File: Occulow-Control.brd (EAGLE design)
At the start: 38.1 x 101.6 mm, 40 parts, among them J1 CORTEX_DEBUG_PTH, T1 DMP3010LK3, T2 DMP3010LK3, T3 DMP3010LK3

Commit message: Move schematic grideye pins to i2c pads, fixes #2
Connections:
- net GR_INT_HDR: now also U$1.13; no longer U$1.14
- net GR_SCL_HDR: now also U$1.12; no longer U$1.13
- net GR_SDA_HDR: now also U$1.11; no longer U$1.12
- net GR_VCC_CTL: now also U$1.14; no longer U$1.11
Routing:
- net GR_INT_HDR: track 16.2 -> 0.00 mm
- net GR_SCL_HDR: track 15.5 -> 0.00 mm
- net GR_SDA_HDR: track 14.8 -> 0.00 mm
- net GR_VCC_CTL: track 11.7 -> 6.48 mm
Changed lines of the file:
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@@
 <signal name="GR_SDA_HDR">
 <contactref element="GRIDEYE_HDR" pad="1"/>
-<contactref element="U$1" pad="12"/>
-<wire x1="21.8165" y1="16.872" x2="23.73" y2="16.872" width="0.254" layer="1"/>
-<wire x1="23.73" y1="16.872" x2="28.321" y2="21.463" width="0.254" layer="1"/>
-<wire x1="28.321" y1="21.463" x2="34.671" y2="21.463" width="0.254" layer="1"/>
-<wire x1="34.671" y1="21.463" x2="34.7345" y2="21.3995" width="0.254" layer="1"/>
+<wire x1="23.73" y1="16.872" x2="28.321" y2="21.463" width="0" layer="19" extent="1-16"/>
+<wire x1="28.321" y1="21.463" x2="34.671" y2="21.463" width="0" layer="19" extent="1-16"/>
+<wire x1="34.671" y1="21.463" x2="34.7345" y2="21.3995" width="0" layer="19" extent="1-16"/>
+<contactref element="U$1" pad="11"/>
+<wire x1="21.8165" y1="16.072" x2="23.73" y2="16.872" width="0" layer="19" extent="1-1"/>
 </signal>
 <signal name="GR_SCL_HDR">
 <contactref element="GRIDEYE_HDR" pad="2"/>
-<contactref element="U$1" pad="13"/>
-<wire x1="21.8165" y1="17.672" x2="23.768" y2="17.672" width="0.254" layer="1"/>
-<wire x1="23.768" y1="17.672" x2="28.194" y2="22.098" width="0.254" layer="1"/>
-<wire x1="28.194" y1="22.098" x2="32.893" y2="22.098" width="0.254" layer="1"/>
-<wire x1="32.893" y1="22.098" x2="34.7345" y2="23.9395" width="0.254" layer="1"/>
+<contactref element="U$1" pad="12"/>
+<wire x1="21.8165" y1="16.872" x2="34.7345" y2="23.9395" width="0" layer="19" extent="1-1"/>
 </signal>
 <signal name="GR_INT_HDR">
 <contactref element="GRIDEYE_HDR" pad="3"/>
-<contactref element="U$1" pad="14"/>
-<wire x1="21.8165" y1="18.472" x2="23.806" y2="18.472" width="0.254" layer="1"/>
-<wire x1="23.806" y1="18.472" x2="27.94" y2="22.606" width="0.254" layer="1"/>
-<wire x1="27.94" y1="22.606" x2="30.861" y2="22.606" width="0.254" layer="1"/>
-<wire x1="30.861" y1="22.606" x2="34.7345" y2="26.4795" width="0.254" layer="1"/>
+<contactref element="U$1" pad="13"/>
+<wire x1="21.8165" y1="17.672" x2="34.7345" y2="26.4795" width="0" layer="19" extent="1-1"/>
 </signal>
 <signal name="GR_VCC_CTL">
 <contactref element="T2" pad="1"/>
-<contactref element="U$1" pad="11"/>
-<wire x1="21.8165" y1="16.072" x2="21.139" y2="16.072" width="0.254" layer="1"/>
-<wire x1="21.139" y1="16.072" x2="20.828" y2="16.383" width="0.254" layer="1"/>
-<wire x1="20.828" y1="16.383" x2="20.828" y2="20.447" width="0.254" layer="1"/>
+<wire x1="21.139" y1="16.072" x2="20.828" y2="16.383" width="0" layer="19" extent="1-16"/>
+<wire x1="20.828" y1="16.383" x2="20.828" y2="20.447" width="0" layer="19" extent="1-16"/>
 <wire x1="20.828" y1="20.447" x2="23.114" y2="22.733" width="0.254" layer="1"/>
 <wire x1="23.114" y1="22.733" x2="23.114" y2="24.531" width="0.254" layer="1"/>
 <wire x1="23.114" y1="24.531" x2="24.136" y2="25.553" width="0.254" layer="1"/>
+<contactref element="U$1" pad="14"/>
+<wire x1="20.828" y1="20.447" x2="21.8165" y2="18.472" width="0" layer="19" extent="1-1"/>
 </signal>
 <signal name="GR_VCC">

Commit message: Updated debug header, re-routed grideye header
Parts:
- removed J1: CORTEX_DEBUG_PTH, SparkFun-Connectors:2X5-PTH-1.27MM
- added U$5: CORTEX-ICE, cortex-debug:2X5-1.27MM
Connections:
- net !RESET: now also U$5.10; no longer J1.10
- net GND: now also U$5.3, U$5.5; no longer J1.3, J1.5
- net SWCLK: now also U$5.4; no longer J1.4
- net SWDIO: now also U$5.2; no longer J1.2
- net VCC: now also U$5.1; no longer J1.1
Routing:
- net GR_INT_HDR: track 0.00 -> 16.6 mm
- net GR_SDA_HDR: track 0.00 -> 16.0 mm
- net GR_SCL_HDR: track 0.00 -> 15.8 mm
- net GR_VCC_CTL: track 6.48 -> 9.30 mm
- net !RESET: track 21.1 -> 21.6 mm
- net SWDIO: track 12.1 -> 11.5 mm
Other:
- board text removed: "CORTEX DEBUG"

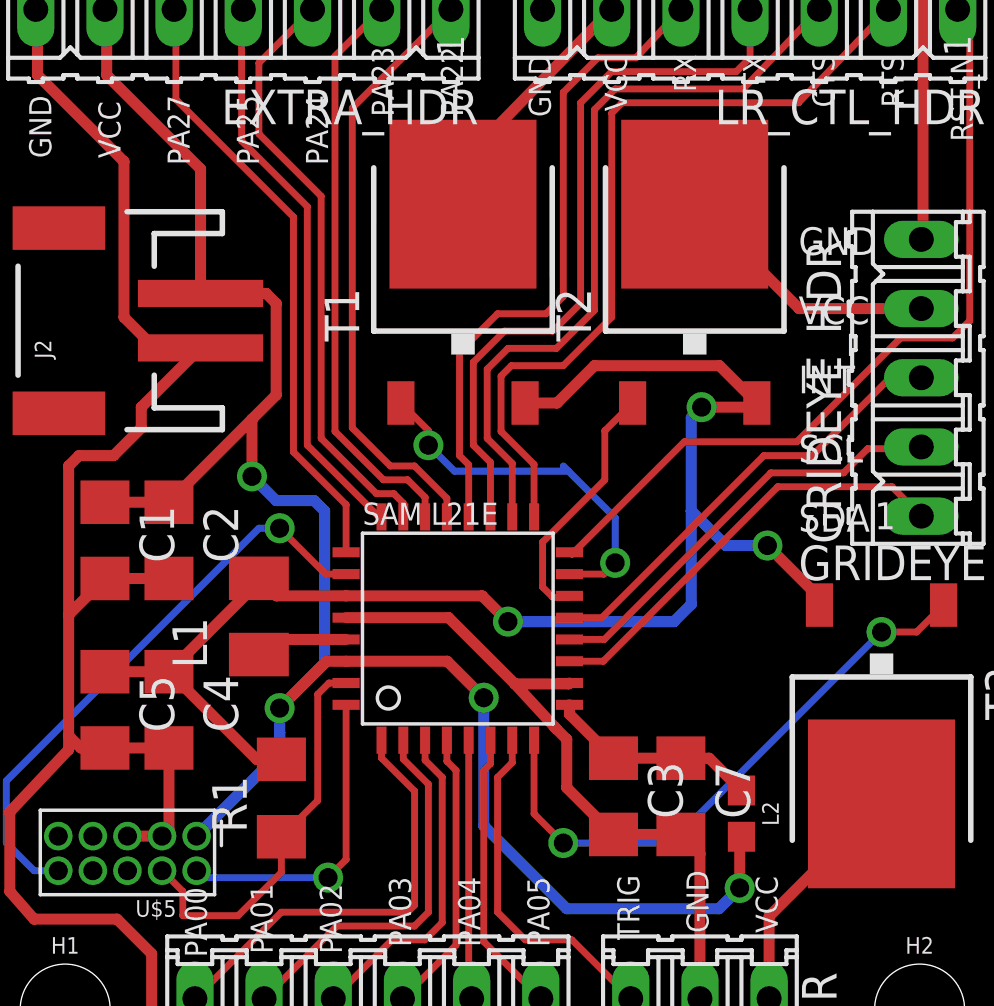
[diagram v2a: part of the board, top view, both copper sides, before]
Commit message: No VDDCORE power, all vcc. Fixes #9
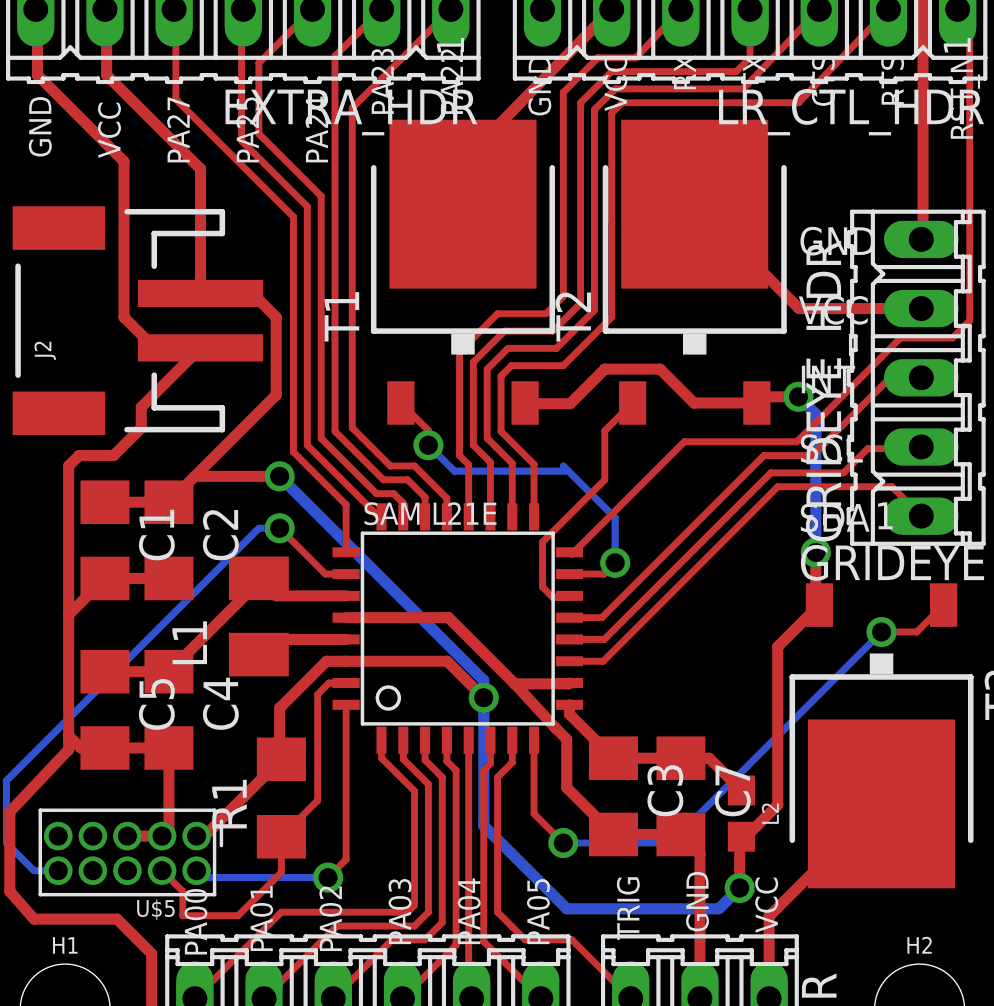
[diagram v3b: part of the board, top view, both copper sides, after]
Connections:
- net VCC: now also R1.2, T1.2, T2.2, T3.2
- net VDDCORE: no longer R1.2, T1.2, T2.2, T3.2
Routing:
- net VDDCORE: track 54.8 -> 10.6 mm, vias 3 -> 0
- net VCC: track 72.0 -> 101.6 mm, vias 4 -> 5
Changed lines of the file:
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@@
 <contactref element="EXTRA_HDR" pad="6"/>
 <wire x1="7.112" y1="21.9105" x2="4.7625" y2="21.9105" width="0.4064" layer="1"/>
-<wire x1="10.684" y1="29.575" x2="8.272" y2="29.575" width="0.4064" layer="1"/>
-<wire x1="10.684" y1="29.575" x2="11.049" y2="29.21" width="0.4064" layer="1"/>
-<wire x1="11.049" y1="29.21" x2="11.049" y2="25.8475" width="0.4064" layer="1"/>
-<wire x1="10.16" y1="24.9585" x2="11.049" y2="25.8475" width="0.4064" layer="1"/>
-<wire x1="10.16" y1="24.9585" x2="7.112" y2="21.9105" width="0.4064" layer="1"/>
-<wire x1="8.272" y1="29.575" x2="8.272" y2="34.146" width="0.4064" layer="1"/>
+<wire x1="8.272" y1="34.146" x2="8.272" y2="29.575" width="0.4064" layer="1"/>
 <wire x1="8.272" y1="34.146" x2="4.826" y2="37.592" width="0.4064" layer="1"/>
 <wire x1="4.826" y1="37.592" x2="4.826" y2="39.9415" width="0.4064" layer="1"/>
 <wire x1="4.826" y1="39.9415" x2="4.7625" y2="40.005" width="0.4064" layer="1"/>
-<wire x1="12.897" y1="16.072" x2="13.6165" y2="16.072" width="0.4064" layer="1"/>
-<wire x1="12.897" y1="16.072" x2="11.176" y2="14.351" width="0.4064" layer="1"/>
-<via x="11.176" y="14.351" extent="1-16" drill="0.7"/>
-<wire x1="11.176" y1="13.081" x2="11.176" y2="13.462" width="0.4064" layer="16"/>
-<via x="10.16" y="22.86" extent="1-16" drill="0.7"/>
-<wire x1="11.176" y1="13.462" x2="11.176" y2="14.351" width="0.4064" layer="16"/>
-<wire x1="10.16" y1="22.86" x2="10.16" y2="24.9585" width="0.4064" layer="1"/>
-<wire x1="11.176" y1="14.351" x2="12.827" y2="16.002" width="0.4064" layer="16"/>
-<wire x1="12.827" y1="16.002" x2="12.827" y2="21.59" width="0.4064" layer="16"/>
-<wire x1="12.827" y1="21.59" x2="12.446" y2="21.971" width="0.4064" layer="16"/>
-<wire x1="12.446" y1="21.971" x2="11.049" y2="21.971" width="0.4064" layer="16"/>
-<wire x1="11.049" y1="21.971" x2="10.16" y2="22.86" width="0.4064" layer="16"/>
-<wire x1="13.6165" y1="16.072" x2="17.329" y2="16.072" width="0.4064" layer="1"/>
+<wire x1="17.329" y1="16.072" x2="13.6165" y2="16.072" width="0.4064" layer="1"/>
 <wire x1="17.329" y1="16.072" x2="18.669" y2="14.732" width="0.4064" layer="1"/>
 <via x="18.669" y="14.732" extent="1-16" drill="0.7"/>
-<wire x1="18.669" y1="14.732" x2="18.669" y2="10.033" width="0.4064" layer="16"/>
+<wire x1="18.669" y1="10.033" x2="18.669" y2="14.732" width="0.4064" layer="16"/>
 <wire x1="18.669" y1="10.033" x2="21.717" y2="6.985" width="0.4064" layer="16"/>
 <wire x1="21.717" y1="6.985" x2="27.305" y2="6.985" width="0.4064" layer="16"/>
@@
 <wire x1="28.067" y1="9.564" x2="28.1305" y2="9.6275" width="0.4064" layer="1"/>
 <contactref element="U$5" pad="1"/>
-<wire x1="11.176" y1="13.462" x2="11.176" y2="12.7" width="0.4064" layer="16"/>
-<wire x1="11.176" y1="12.7" x2="8.128" y2="9.652" width="0.4064" layer="16"/>
+<contactref element="R1" pad="2"/>
+<contactref element="T1" pad="2"/>
+<contactref element="T2" pad="2"/>
+<contactref element="T3" pad="2"/>
+<wire x1="28.1305" y1="9.6275" x2="28.2965" y2="9.6275" width="0.4064" layer="1"/>
+<wire x1="28.2965" y1="9.6275" x2="29.464" y2="10.795" width="0.4064" layer="1"/>
+<wire x1="29.464" y1="10.795" x2="29.464" y2="16.605" width="0.4064" layer="1"/>
+<wire x1="30.994" y1="18.135" x2="29.464" y2="16.605" width="0.4064" layer="1"/>
+<wire x1="8.272" y1="29.575" x2="10.176" y2="29.575" width="0.4064" layer="1"/>
+<wire x1="10.176" y1="29.575" x2="11.049" y2="28.702" width="0.4064" layer="1"/>
+<wire x1="11.049" y1="28.702" x2="11.049" y2="25.8475" width="0.4064" layer="1"/>
+<wire x1="8.0615" y1="22.86" x2="11.049" y2="25.8475" width="0.4064" layer="1"/>
+<wire x1="8.0615" y1="22.86" x2="7.112" y2="21.9105" width="0.4064" layer="1"/>
+<wire x1="13.6165" y1="16.072" x2="12.897" y2="16.072" width="0.4064" layer="1"/>
+<wire x1="12.897" y1="16.072" x2="11.176" y2="14.351" width="0.4064" layer="1"/>
+<wire x1="11.176" y1="14.351" x2="11.176" y2="12.5345" width="0.4064" layer="1"/>
+<wire x1="11.2395" y1="12.471" x2="11.176" y2="12.5345" width="0.4064" layer="1"/>
+<wire x1="8.128" y1="9.652" x2="8.4205" y2="9.652" width="0.4064" layer="1"/>
+<wire x1="8.4205" y1="9.652" x2="11.2395" y2="12.471" width="0.4064" layer="1"/>
+<via x="30.861" y="20.066" extent="1-16" drill="0.7"/>
+<wire x1="30.861" y1="20.066" x2="30.861" y2="18.268" width="0.4064" layer="1"/>
+<wire x1="30.861" y1="18.268" x2="30.994" y2="18.135" width="0.4064" layer="1"/>
+<wire x1="30.861" y1="20.066" x2="30.861" y2="25.146" width="0.4064" layer="16"/>
+<wire x1="30.861" y1="25.146" x2="30.226" y2="25.781" width="0.4064" layer="16"/>
+<via x="30.226" y="25.781" extent="1-16" drill="0.7"/>
+<wire x1="30.226" y1="25.781" x2="28.924" y2="25.781" width="0.4064" layer="1"/>
+<wire x1="28.924" y1="25.781" x2="28.696" y2="25.553" width="0.4064" layer="1"/>
+<wire x1="28.696" y1="25.553" x2="26.39" y2="25.553" width="0.4064" layer="1"/>
+<wire x1="26.39" y1="25.553" x2="25.146" y2="26.797" width="0.4064" layer="1"/>
+<wire x1="25.146" y1="26.797" x2="23.114" y2="26.797" width="0.4064" layer="1"/>
+<wire x1="23.114" y1="26.797" x2="21.844" y2="25.527" width="0.4064" layer="1"/>
+<wire x1="21.844" y1="25.527" x2="20.213" y2="25.527" width="0.4064" layer="1"/>
+<wire x1="20.213" y1="25.527" x2="20.187" y2="25.553" width="0.4064" layer="1"/>
+<wire x1="18.669" y1="14.732" x2="18.669" y2="15.367" width="0.4064" layer="16"/>
+<via x="11.176" y="22.86" extent="1-16" drill="0.7"/>
+<wire x1="11.176" y1="22.86" x2="8.0615" y2="22.86" width="0.4064" layer="1"/>
+<wire x1="18.669" y1="15.367" x2="11.176" y2="22.86" width="0.4064" layer="16"/>
 </signal>
 <signal name="RF">
@@
 <contactref element="U$1" pad="27"/>
 <contactref element="C4" pad="1"/>
-<contactref element="T1" pad="2"/>
-<contactref element="T2" pad="2"/>
-<contactref element="T3" pad="2"/>
 <contactref element="L1" pad="2"/>
 <wire x1="11.0585" y1="18.472" x2="13.6165" y2="18.472" width="0.4064" layer="1"/>
 <wire x1="11.0585" y1="18.472" x2="10.414" y2="19.1165" width="0.4064" layer="1"/>
-<contactref element="R1" pad="2"/>
 <wire x1="7.112" y1="15.6875" x2="4.7625" y2="15.6875" width="0.4064" layer="1"/>
 <wire x1="10.414" y1="19.1165" x2="10.414" y2="18.9895" width="0.4064" layer="1"/>
 <wire x1="10.414" y1="18.9895" x2="7.112" y2="15.6875" width="0.4064" layer="1"/>
-<wire x1="11.2395" y1="12.471" x2="10.3285" y2="12.471" width="0.4064" layer="1"/>
-<wire x1="10.3285" y1="12.471" x2="7.112" y2="15.6875" width="0.4064" layer="1"/>
-<wire x1="20.187" y1="25.553" x2="21.362" y2="25.553" width="0.4064" layer="1"/>
-<wire x1="21.362" y1="25.553" x2="22.733" y2="26.924" width="0.4064" layer="1"/>
-<wire x1="22.733" y1="26.924" x2="27.325" y2="26.924" width="0.4064" layer="1"/>
-<wire x1="28.696" y1="25.553" x2="27.325" y2="26.924" width="0.4064" layer="1"/>
-<wire x1="13.6165" y1="18.472" x2="18.612" y2="18.472" width="0.4064" layer="1"/>
-<wire x1="18.612" y1="18.472" x2="19.558" y2="17.526" width="0.4064" layer="1"/>
-<via x="19.558" y="17.526" extent="1-16" drill="0.7"/>
-<wire x1="19.558" y1="17.526" x2="25.654" y2="17.526" width="0.4064" layer="16"/>
-<wire x1="25.654" y1="17.526" x2="26.289" y2="18.161" width="0.4064" layer="16"/>
-<wire x1="26.289" y1="21.59" x2="26.289" y2="18.161" width="0.4064" layer="16"/>
-<wire x1="26.289" y1="21.59" x2="26.289" y2="25.019" width="0.4064" layer="16"/>
-<wire x1="26.289" y1="25.019" x2="26.67" y2="25.4" width="0.4064" layer="16"/>
-<via x="26.67" y="25.4" extent="1-16" drill="0.7"/>
-<wire x1="26.67" y1="25.4" x2="28.543" y2="25.4" width="0.4064" layer="1"/>
-<wire x1="28.543" y1="25.4" x2="28.696" y2="25.553" width="0.4064" layer="1"/>
-<wire x1="30.994" y1="18.135" x2="30.994" y2="18.409" width="0.4064" layer="1"/>
-<wire x1="30.994" y1="18.409" x2="29.083" y2="20.32" width="0.4064" layer="1"/>
-<via x="29.083" y="20.32" extent="1-16" drill="0.7"/>
-<wire x1="29.083" y1="20.32" x2="27.559" y2="20.32" width="0.4064" layer="16"/>
-<wire x1="27.559" y1="20.32" x2="26.289" y2="21.59" width="0.4064" layer="16"/>
 </signal>
 <signal name="LR_RX_HDR">
